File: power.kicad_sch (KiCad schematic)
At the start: 60 parts, among them U10 MAX4995AAUT, U11 MAX4995AAUT, U35 MAX4995AAUT, U4 TPSM828302ARDSR, U5 LP3962EMP-3.3/NOPB, U6 STWD100NYWY3F, U8 MP5073GG-P, U9 MAX4995AAUT

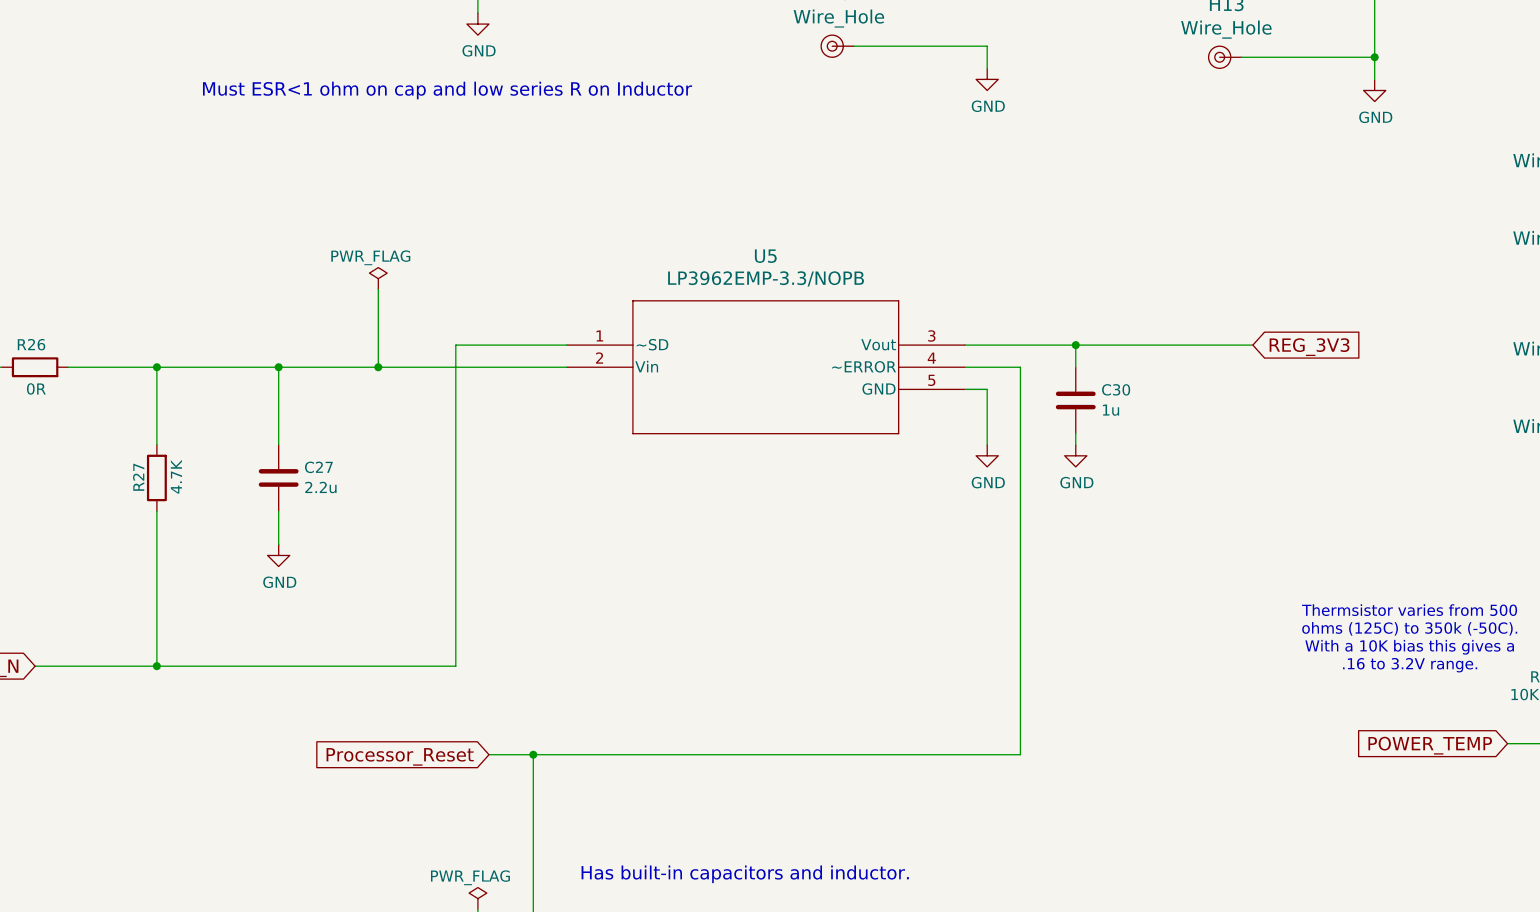
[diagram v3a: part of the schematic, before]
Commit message: Change 3.3V power convert to a TPS7A52-Q1
It's AEC rated.

Signed-off-by: Corey Minyard <corey@minyard.net>
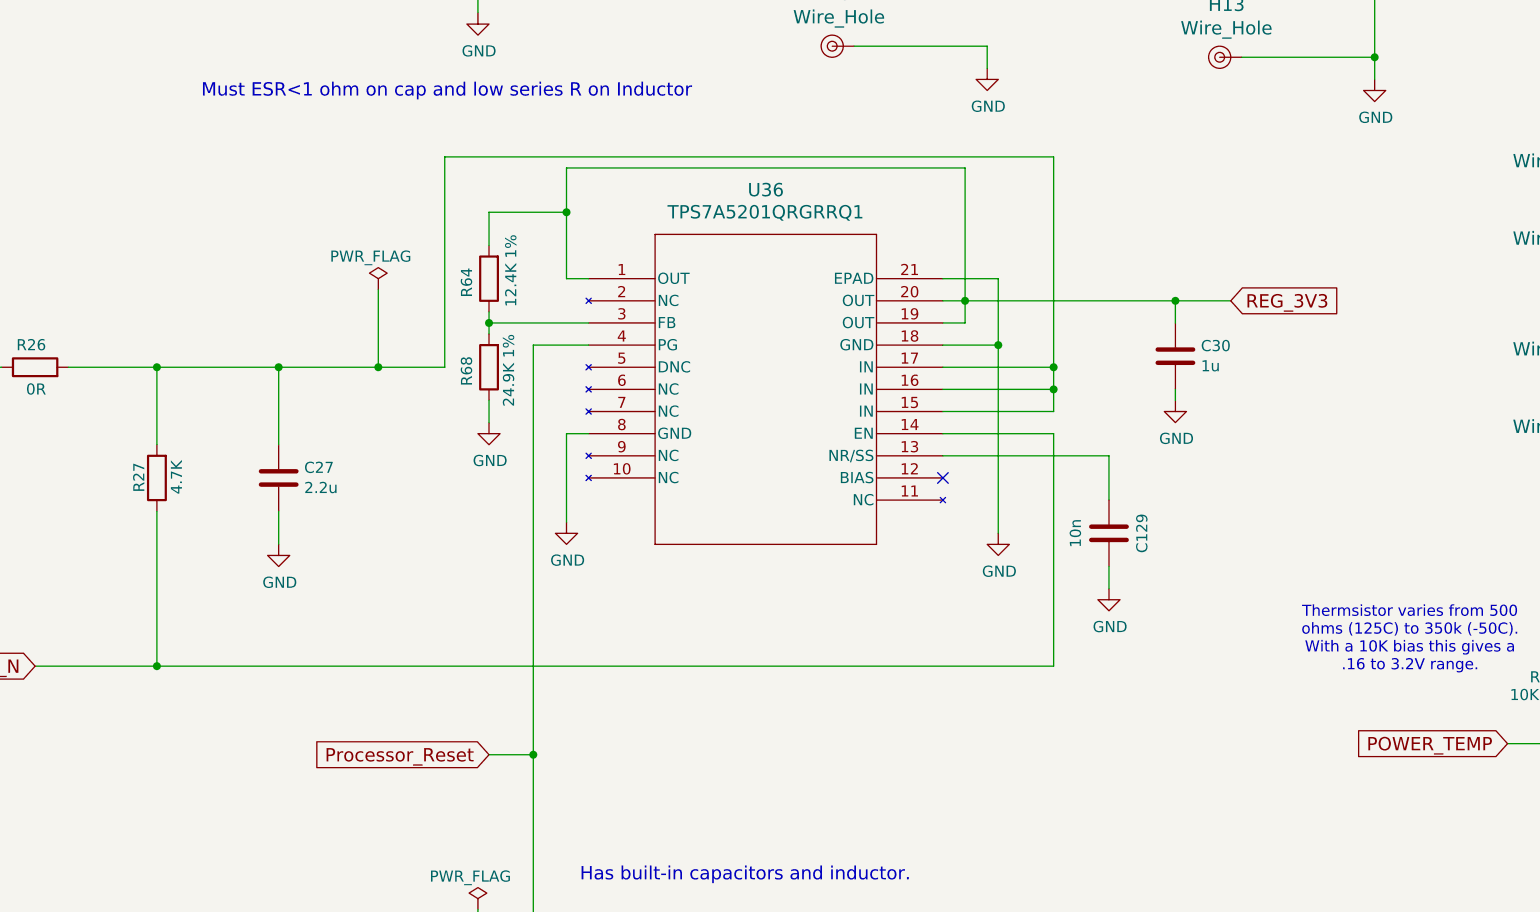
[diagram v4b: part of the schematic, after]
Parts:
- removed U5: LP3962EMP-3.3/NOPB, PacSatDev_ti:MP05A, symbol PACSAT_ICs:LP3962EMP-3.3_NOPB
- added C129: 10n, Capacitor_SMD:C_0402_1005Metric_Pad0.74x0.62mm_HandSolder, symbol Device:C
- added R64: 12.4K 1%, Resistor_SMD:R_0402_1005Metric_Pad0.72x0.64mm_HandSolder, symbol Device:R
- added R68: 24.9K 1%, Resistor_SMD:R_0402_1005Metric_Pad0.72x0.64mm_HandSolder, symbol Device:R
- added U36: TPS7A5201QRGRRQ1, PacSatDev_ti:RGR20_2P05X2P05_TEX, symbol PACSAT_ICs:TPS7A5201QRGRRQ1
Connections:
- net GND: now also C129.2, R68.1, U36.18 (GND), U36.21 (EPAD), U36.8 (GND)
- net HW_POWER_OFF_N: now also U36.14 (EN)
- net Processor_Reset: now also U36.4 (PG)
- net REG_3V3: now also R64.2, U36.1 (OUT), U36.19 (OUT), U36.20 (OUT)
- net at C27.1, R26.2, R27.2: now also U36.15 (IN), U36.16 (IN), U36.17 (IN)
- new net: C129.1, U36.13 (NR/SS)
- new net: R64.1, R68.2, U36.3 (FB)
- no-connect marks 2 -> 3
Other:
- moved on the sheet: C30

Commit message: Work on cleaning up all values for things
Signed-off-by: Corey Minyard <corey@minyard.net>
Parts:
- H10, H11, H12, H13, H14, H15, H16, H17, H6, H7, H8, H9, JP2: now left out of the parts list
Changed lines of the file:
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@@
 		(unit 1)
 		(exclude_from_sim no)
-		(in_bom yes)
+		(in_bom no)
 		(on_board yes)
 		(dnp no)
@@
 		(unit 1)
 		(exclude_from_sim no)
-		(in_bom yes)
+		(in_bom no)
 		(on_board yes)
 		(dnp no)
@@
 		(unit 1)
 		(exclude_from_sim no)
-		(in_bom yes)
+		(in_bom no)
 		(on_board yes)
 		(dnp no)
@@
 		(unit 1)
 		(exclude_from_sim no)
-		(in_bom yes)
+		(in_bom no)
 		(on_board yes)
 		(dnp no)
@@
 		(unit 1)
 		(exclude_from_sim no)
-		(in_bom yes)
+		(in_bom no)
 		(on_board yes)
 		(dnp no)
@@
 		(unit 1)
 		(exclude_from_sim no)
-		(in_bom yes)
+		(in_bom no)
 		(on_board yes)
 		(dnp no)
@@
 		(unit 1)
 		(exclude_from_sim no)
-		(in_bom yes)
+		(in_bom no)
 		(on_board yes)
 		(dnp no)
@@
 		(unit 1)
 		(exclude_from_sim no)
-		(in_bom yes)
+		(in_bom no)
 		(on_board yes)
 		(dnp no)
@@
 		(unit 1)
 		(exclude_from_sim no)
-		(in_bom yes)
+		(in_bom no)
 		(on_board yes)
 		(dnp no)
@@
 		(unit 1)
 		(exclude_from_sim no)
-		(in_bom yes)
+		(in_bom no)
 		(on_board yes)
 		(dnp no)
@@
 		(unit 1)
 		(exclude_from_sim no)
-		(in_bom yes)
+		(in_bom no)
 		(on_board yes)
 		(dnp no)
@@
 		(unit 1)
 		(exclude_from_sim no)
-		(in_bom yes)
+		(in_bom no)
 		(on_board yes)
 		(dnp no)
@@
 		(unit 1)
 		(exclude_from_sim no)
-		(in_bom yes)
+		(in_bom no)
 		(on_board yes)
 		(dnp no)

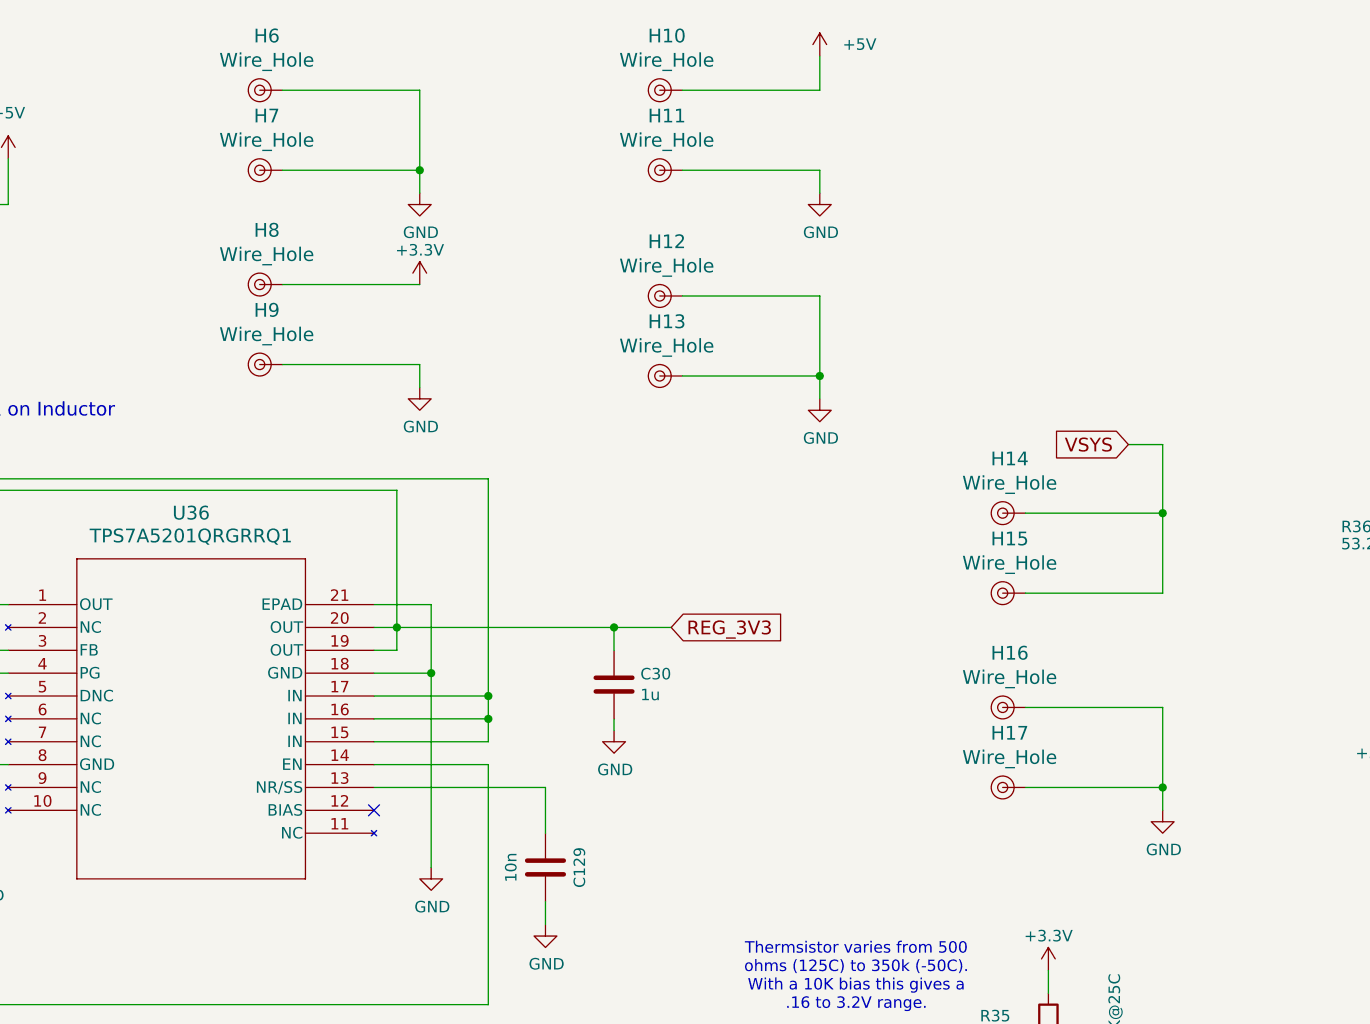
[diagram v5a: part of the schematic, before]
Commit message: More work on components
Signed-off-by: Corey Minyard <corey@minyard.net>
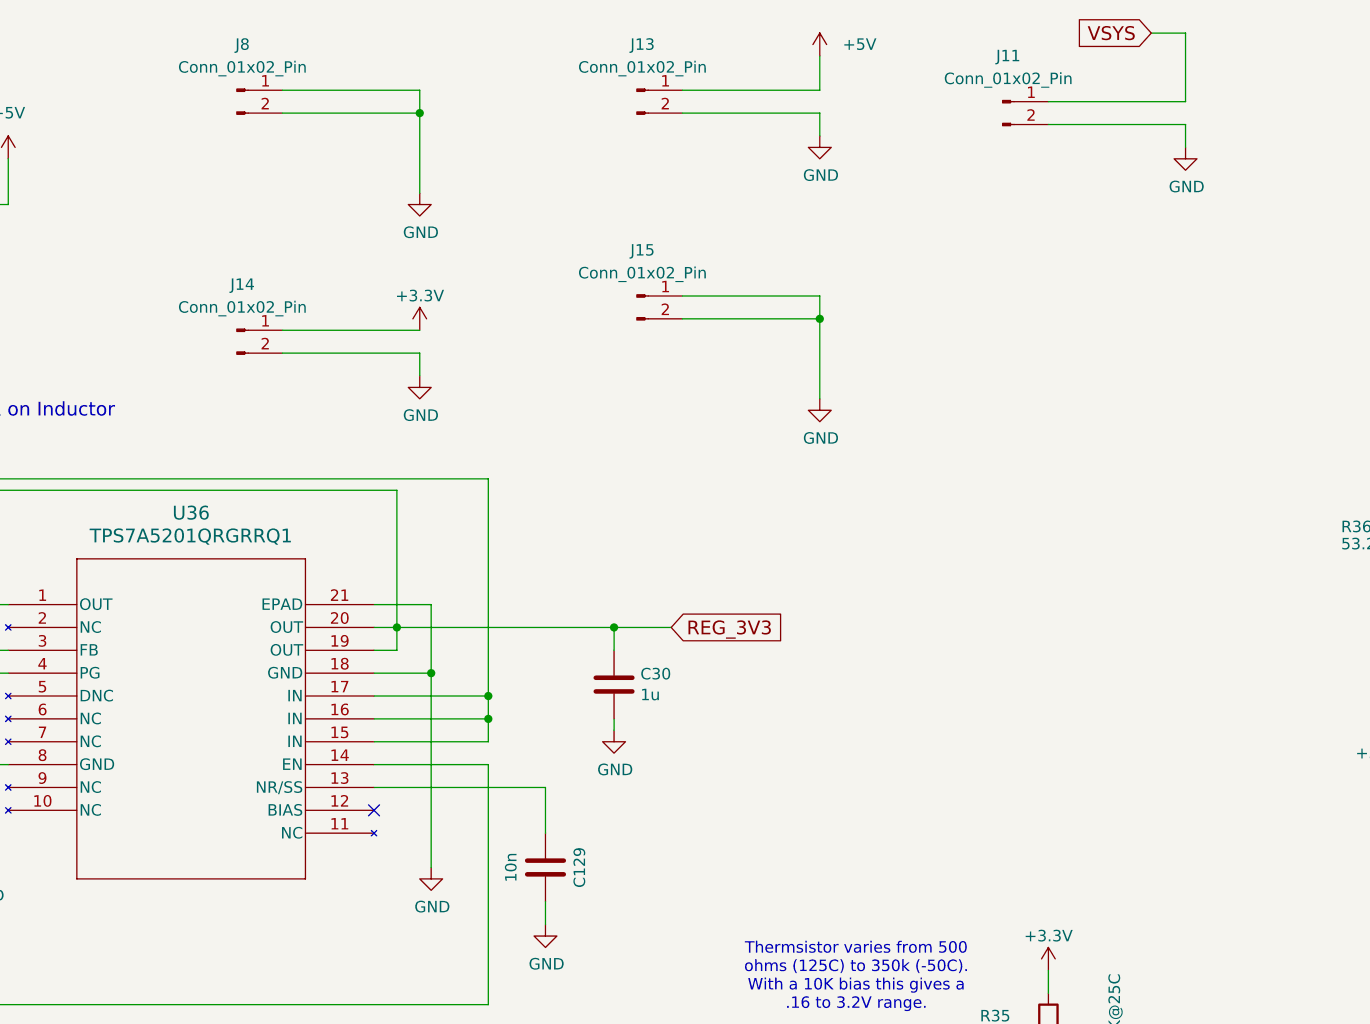
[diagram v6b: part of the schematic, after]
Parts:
- removed H10, H11, H12, H13, H14, H15, H16, H17, H6, H7, H8, H9: Wire_Hole, PacSatDev_misc:Wire_Hole, symbol PACSAT_DEV_misc:CUBESAT_MOUNT_HOLE_1
- added J11, J13, J14, J15, J8: Conn_01x02_Pin, Connector_Wire:SolderWire-0.5sqmm_1x02_P4.6mm_D0.9mm_OD2.1mm, symbol Connector:Conn_01x02_Pin
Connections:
- net +3.3V: now also J14.1 (Pin_1)
- net +5V: now also J13.1 (Pin_1)
- net GND: now also J11.2 (Pin_2), J13.2 (Pin_2), J14.2 (Pin_2), J15.1 (Pin_1), J15.2 (Pin_2), J8.1 (Pin_1), J8.2 (Pin_2)
- net VSYS: now also J11.1 (Pin_1)
